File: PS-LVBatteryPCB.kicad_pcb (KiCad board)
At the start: 2 copper layers, 7 parts, among them J1 NTC_01, J2 NTC_02, J3 NTC_OUT, J4 SUPP+, J5 SUPP_GND, J6 SUPP_FUSE

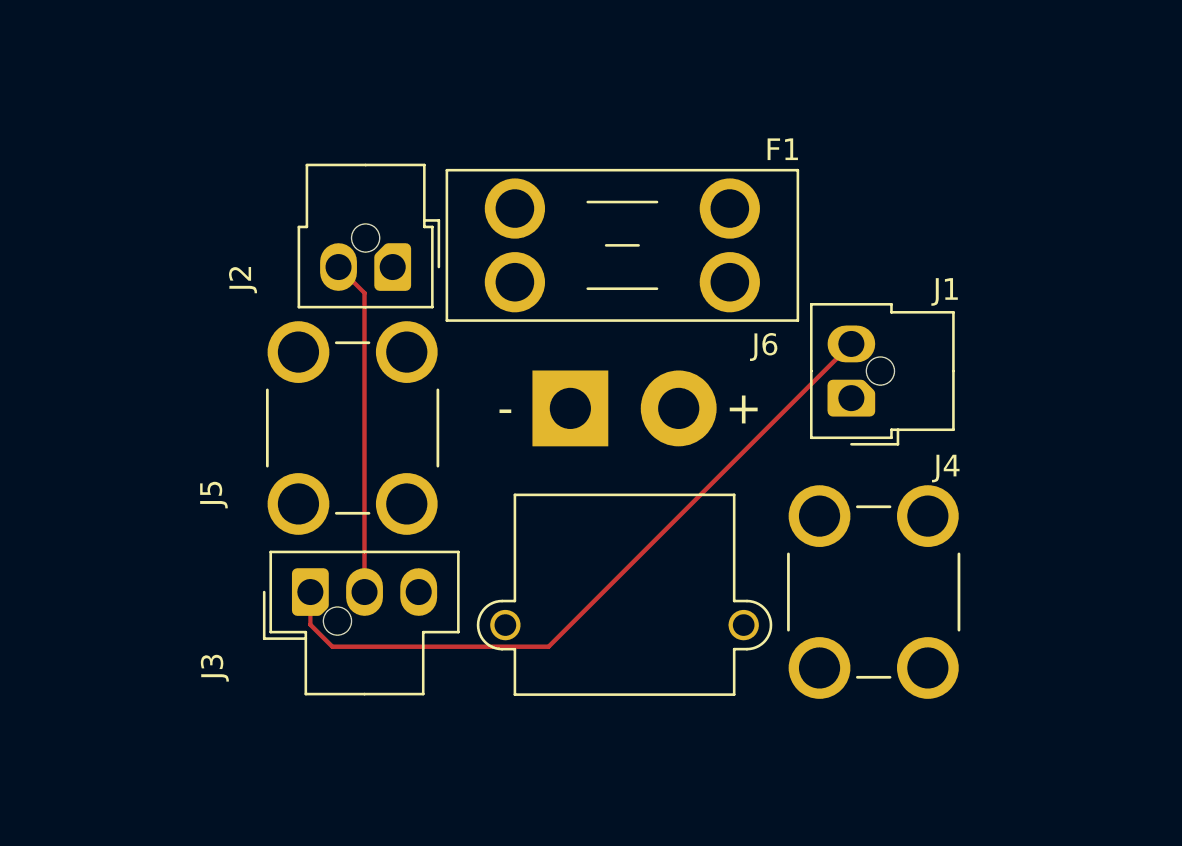
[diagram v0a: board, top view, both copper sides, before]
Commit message: Added all fp's, added edge and planes, added traces, lots of errors
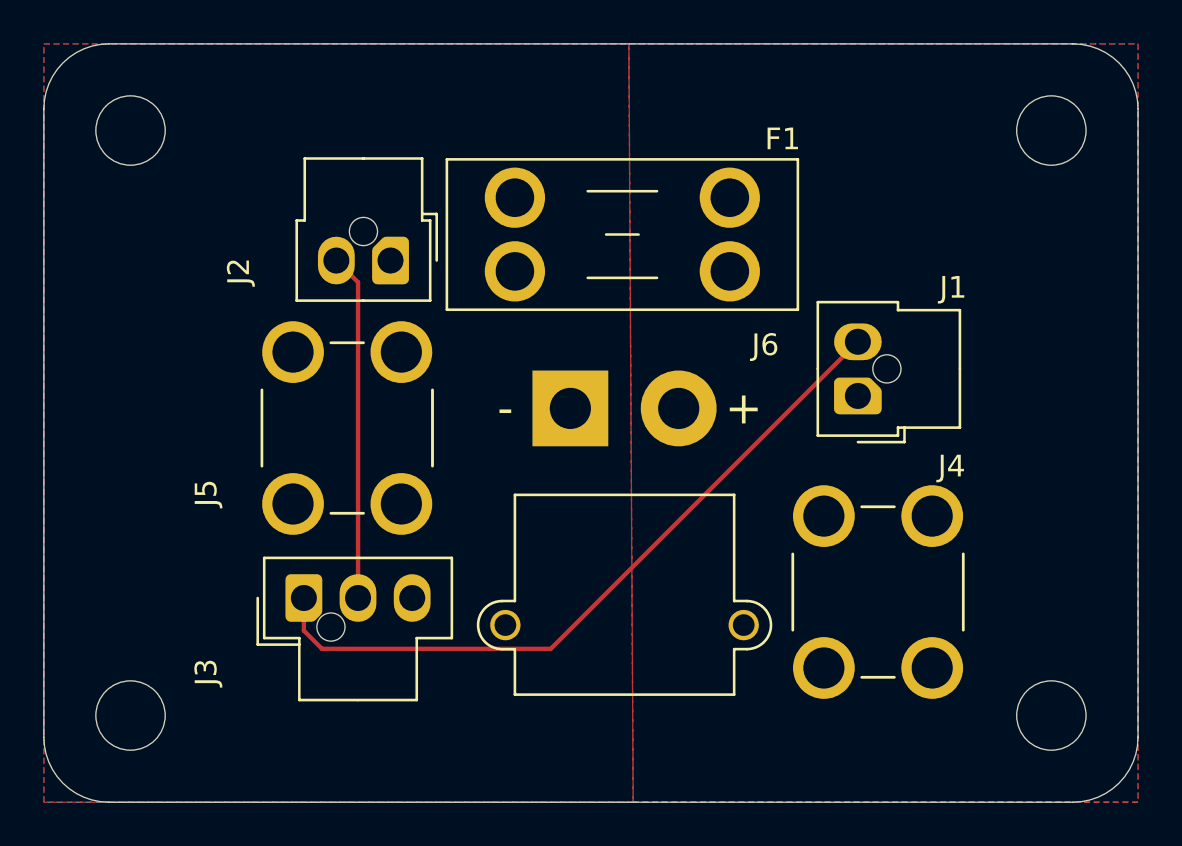
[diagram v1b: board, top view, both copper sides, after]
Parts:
- added REF**: MountingHole_3.2mm_M3, MountingHole:MountingHole_3.2mm_M3, F.Cu at (164.0, 109.5)
- added REF**: MountingHole_3.2mm_M3, MountingHole:MountingHole_3.2mm_M3, F.Cu at (121.5, 82.5)
- added REF**: MountingHole_3.2mm_M3, MountingHole:MountingHole_3.2mm_M3, F.Cu at (121.5, 109.5)
- added REF**: MountingHole_3.2mm_M3, MountingHole:MountingHole_3.2mm_M3, F.Cu at (164.0, 82.5)
- moved F1 0.50 mm to (139.2, 85.6)
- moved J3 0.41 mm to (129.5, 104.1)
- moved J2 0.32 mm to (133.5, 88.5)
- moved J1 0.32 mm to (155.1, 94.8)
- moved J5 0.25 mm to (131.5, 96.2)
- moved J4 0.20 mm to (156.0, 103.8)
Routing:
- net Net-(J1-Pin_2): track 32.7 -> 33.3 mm
- added copper zone on F.Cu, net /SUPP+
- added copper zone on F.Cu, net /SUPP_FUSE+
- added copper zone on B.Cu, net /SUPP_GND
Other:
- board outline added: 50.5 x 35 mm

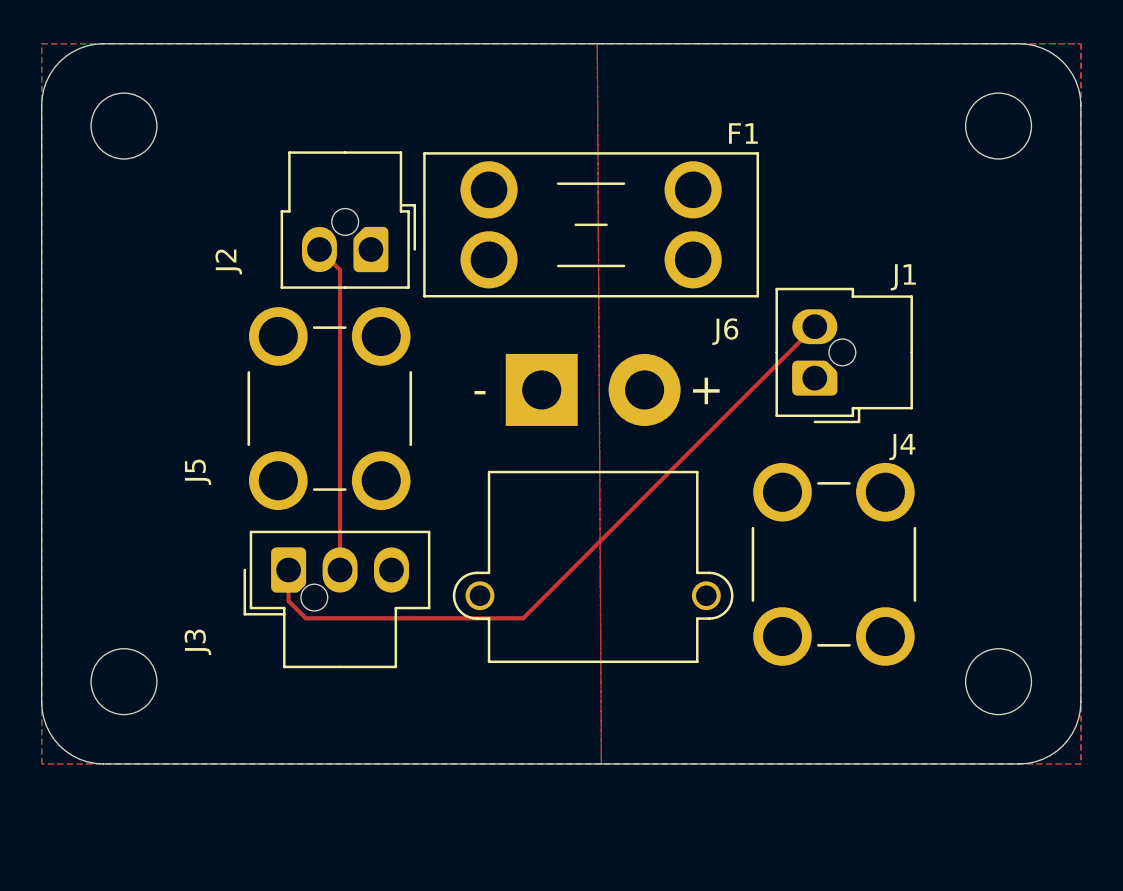
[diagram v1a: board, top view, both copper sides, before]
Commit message: reorganized pcb and changed up fp's
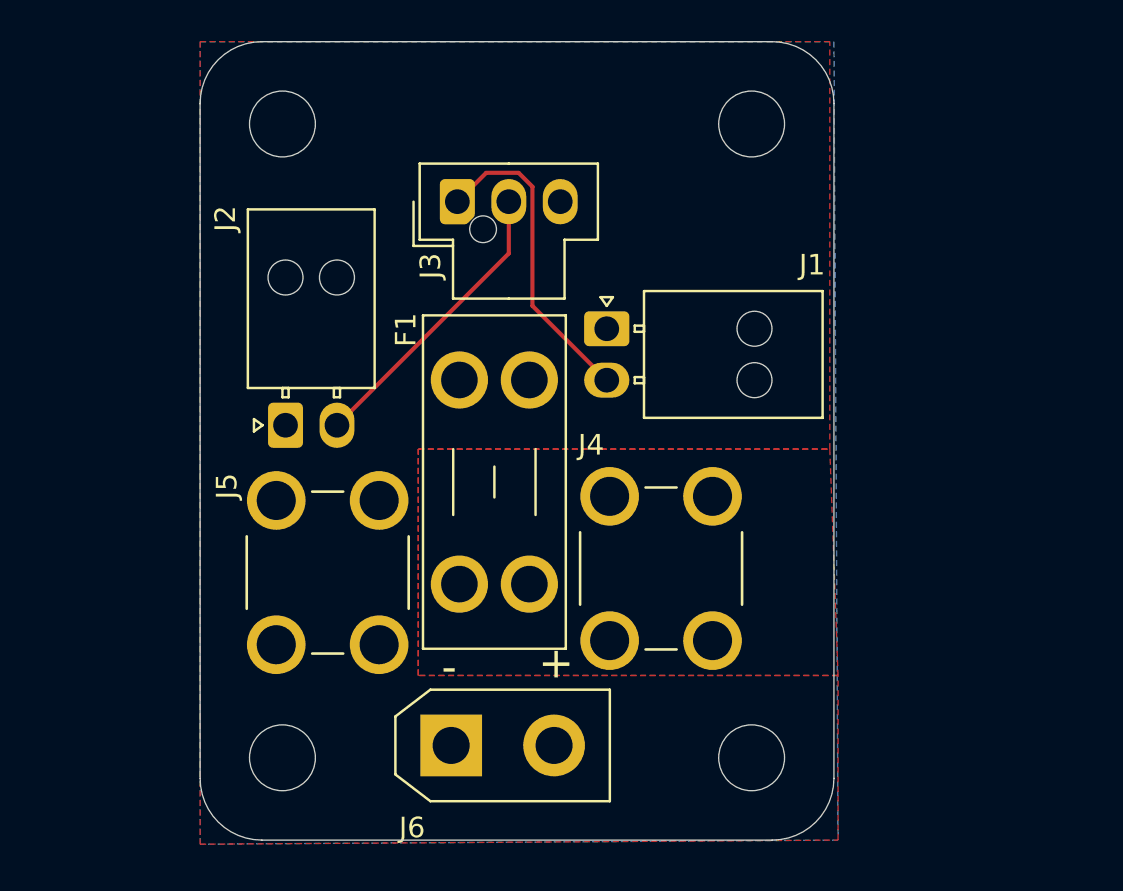
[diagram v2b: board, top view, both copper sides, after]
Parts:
- J1, J2: footprint UTSVT_Connectors:Molex_Nano-Fit_105309-xx02_1x02_P2.50mm_Vertical -> Connector_Molex:Molex_Nano-Fit_105313-xx02_1x02_P2.50mm_Horizontal
- J6: footprint UTSVT_Connectors:AMASS_XT30PW-M_1x02_P2.50mm_Horizontal -> UTSVT_Connectors:AMASS_XT30UPB-M_1x02_P5.0mm_Vertical
- moved J3 19.7 mm to (137.7, 86.2)
- moved J6 17.8 mm to (137.4, 112.6), turned to 0 degrees
- moved REF** 12.6 mm to (152.0, 113.2)
- moved REF** 12.0 mm to (152.0, 82.4)
- moved J1 10.4 mm to (145.0, 92.3), turned to 0 degrees
- moved J2 9.49 mm to (129.3, 97.0), turned to 90 degrees
- moved F1 9.45 mm to (141.2, 94.8), turned to -90 degrees
- moved REF** 8.54 mm to (129.2, 113.2)
- moved J4 8.40 mm to (147.6, 104.0)
- moved J5 7.97 mm to (131.4, 104.2)
- moved REF** 7.70 mm to (129.2, 82.4)
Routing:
- net Net-(J1-Pin_2): track 33.3 -> 15.4 mm
- net Net-(J2-Pin_2): track 16.0 -> 14.3 mm
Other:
- board size 50.5 x 35 mm -> 30.8 x 38.8 mm

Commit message: reorganize and added SOME 3D models
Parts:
- moved J1 11.8 mm to (145.0, 104.2)
- moved REF** 10.0 mm to (139.0, 80.2)
- moved J4 9.85 mm to (151.6, 95.0)
- moved REF** 2.20 mm to (152.0, 80.2)
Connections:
- F1 pad 1: /SUPP_FUSE+ -> /SUPP+
- F1 pad 2: /SUPP+ -> /SUPP_FUSE+
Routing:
- net Net-(J1-Pin_2): track 15.4 -> 27.2 mm
- removed copper zone on F.Cu, net /SUPP+
- removed copper zone on F.Cu, net /SUPP_FUSE+
- removed copper zone on B.Cu, net /SUPP_GND
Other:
- board size 30.8 x 38.8 mm -> 30.8 x 41 mm

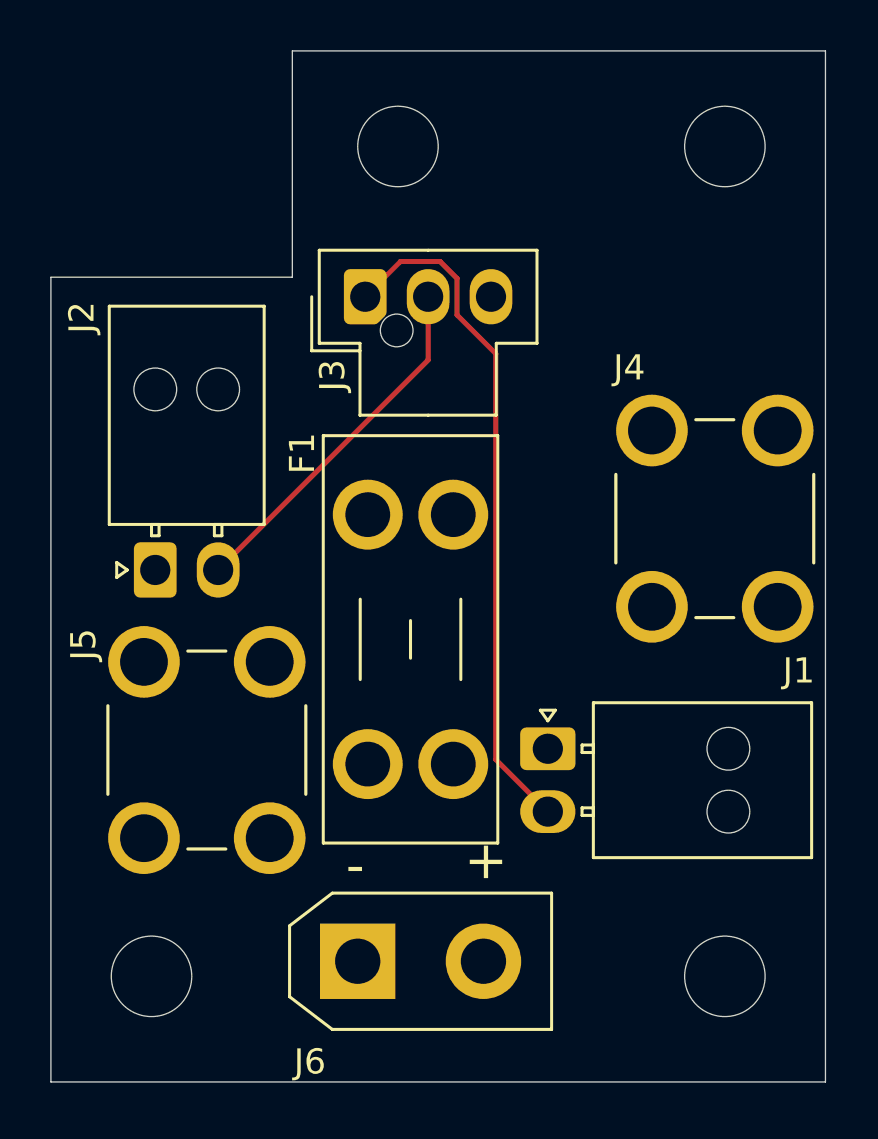
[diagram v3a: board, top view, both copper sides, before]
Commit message: reorganized layout, gotta add planes
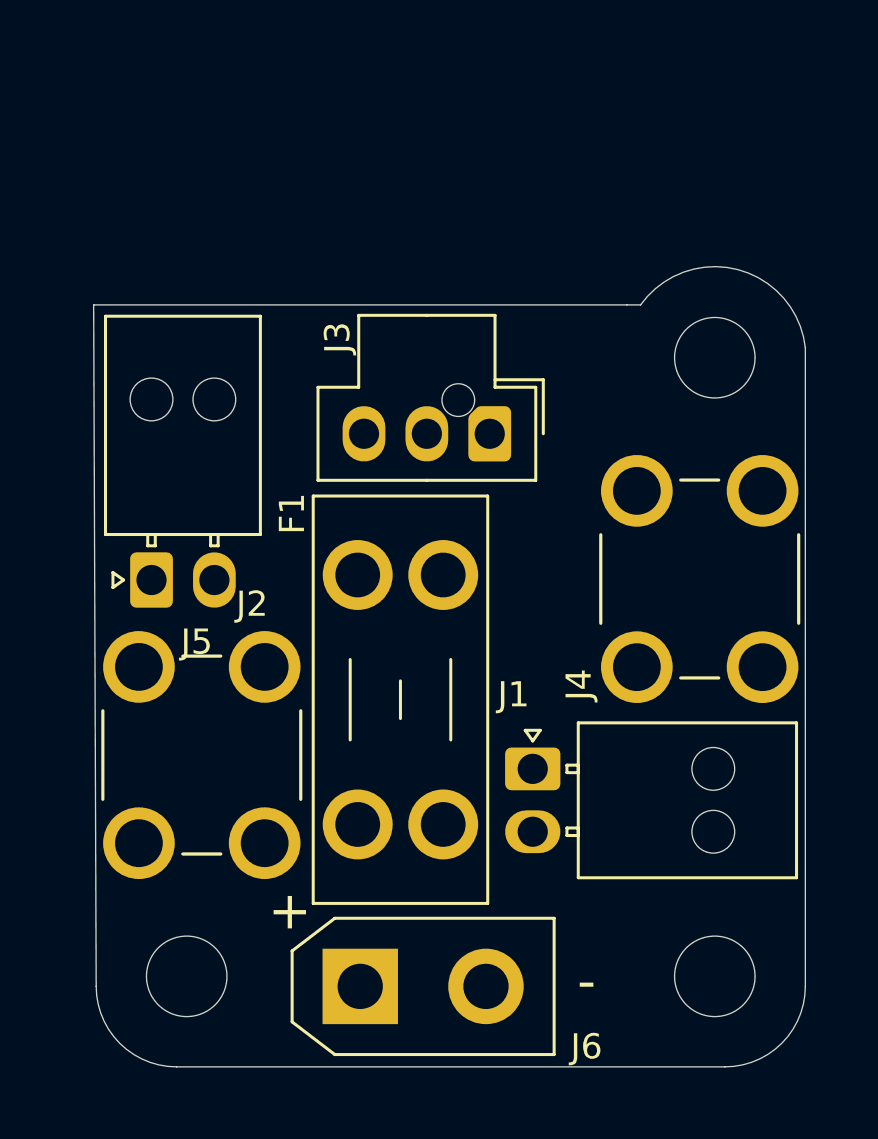
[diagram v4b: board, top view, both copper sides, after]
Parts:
- removed the REF** at (139.0, 80.2)
- moved REF** 8.41 mm to (151.6, 88.6)
- moved J3 7.36 mm to (142.7, 91.6), turned to -90 degrees
- moved J4 2.47 mm to (151.0, 97.4)
- moved F1 2.43 mm to (140.8, 97.2)
- moved REF** 1.40 mm to (130.6, 113.2)
- moved J6 1.00 mm to (137.5, 113.6)
- moved J1 1.00 mm to (144.4, 105.0)
- moved J2 0.43 mm to (129.2, 97.4)
- moved REF** 0.40 mm to (151.6, 113.2)
- moved J5 0.28 mm to (131.2, 104.4)
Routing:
- net Net-(J1-Pin_2): track 27.2 -> 0.00 mm
- net Net-(J2-Pin_2): track 14.3 -> 0.00 mm
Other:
- board size 30.8 x 41 mm -> 28.3 x 31.8 mm

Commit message: R1
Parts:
- moved REF** 0.26 mm to (130.7, 113.0)
- moved REF** 0.22 mm to (151.5, 113.0)
- moved J1 0.19 mm to (144.2, 104.8)
- moved REF** 0.16 mm to (151.6, 88.8)
- moved F1 0.10 mm to (140.7, 97.2)
- moved J5 0.10 mm to (131.2, 104.3)
- moved J3 0.09 mm to (142.6, 91.7)
- moved J4 0.07 mm to (150.9, 97.4)
- moved J2 0.07 mm to (129.2, 97.5)
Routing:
- net Net-(J1-Pin_2): track 0.00 -> 37.2 mm
- net Net-(J1-Pin_1): track 0.00 -> 31.7 mm
- net Net-(J2-Pin_2): track 0.00 -> 11.9 mm
- added copper zone on F.Cu, net /SUPP+
- added copper zone on F.Cu, net /SUPP_FUSE+
- added copper zone on B.Cu, net /SUPP_GND
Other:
- board size 28.3 x 31.8 mm -> 28.2 x 31.4 mm

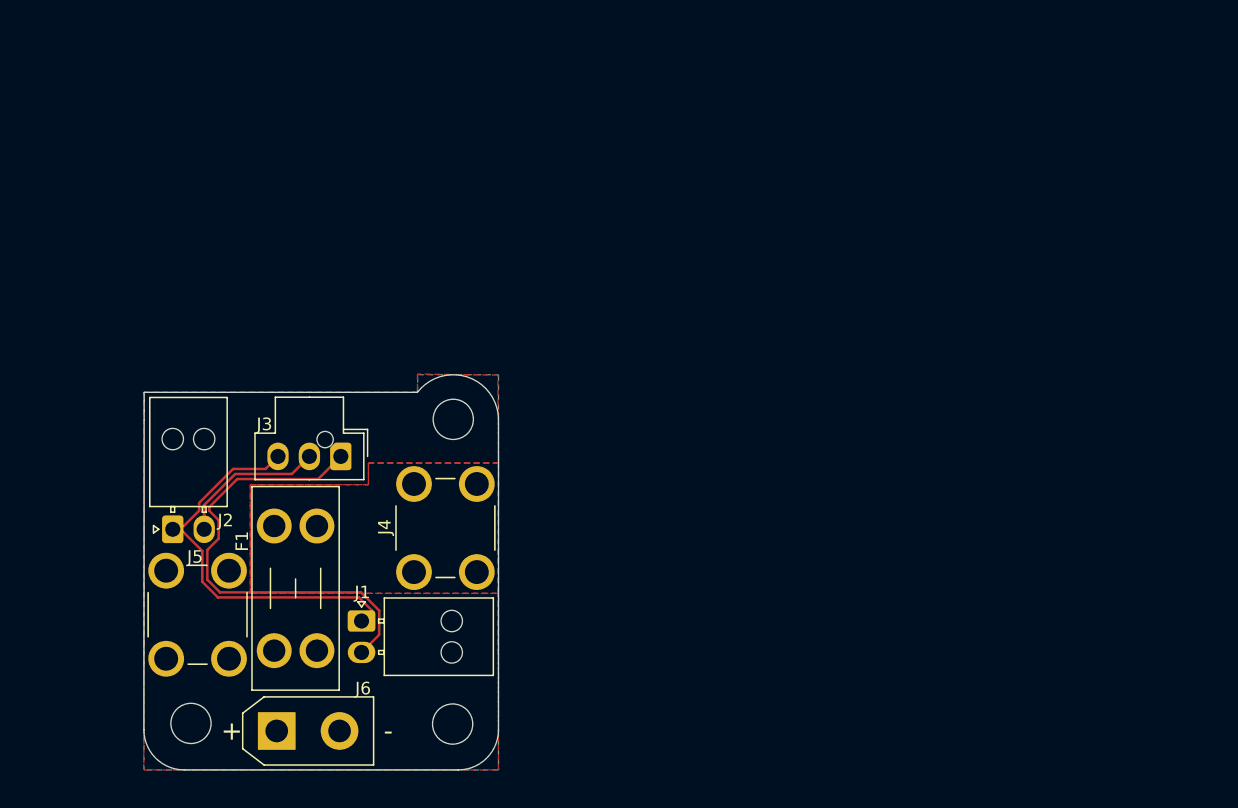
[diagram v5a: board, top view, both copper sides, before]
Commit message: thinner layout
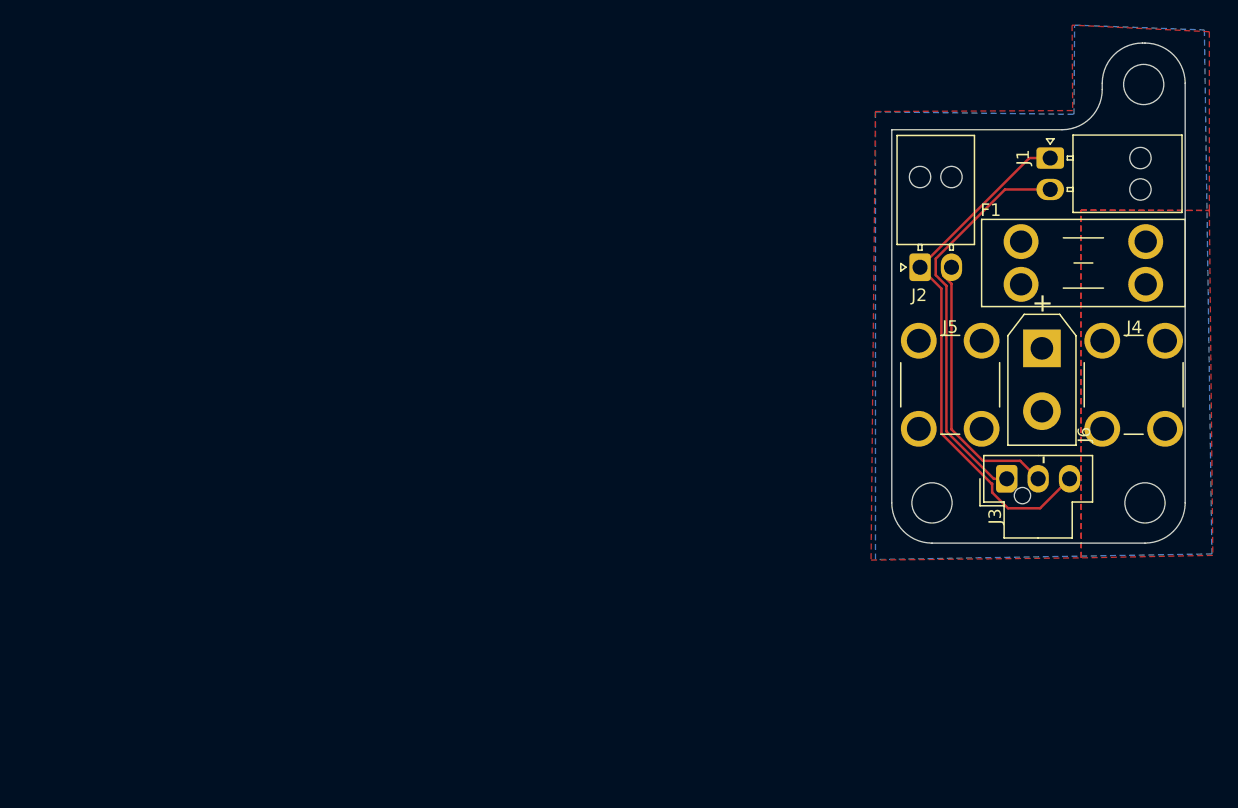
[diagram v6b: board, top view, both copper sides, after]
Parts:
- moved REF** 77.9 mm to (206.6, 95.4)
- moved F1 68.7 mm to (206.7, 78.0), turned to 180 degrees
- moved J6 68.1 mm to (198.4, 83.1), turned to -90 degrees
- moved J1 66.0 mm to (199.1, 68.0)
- moved J2 63.0 mm to (188.7, 76.6)
- moved J5 62.6 mm to (191.1, 86.0)
- moved REF** 61.1 mm to (206.5, 62.1)
- moved J4 55.9 mm to (205.7, 86.0)
- moved J3 53.0 mm to (195.6, 93.5), turned to 90 degrees
- moved REF** 42.0 mm to (189.7, 95.4)
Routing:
- net Net-(J1-Pin_1): track 31.7 -> 41.9 mm
- net Net-(J2-Pin_2): track 11.9 -> 22.0 mm
- net Net-(J1-Pin_2): track 37.2 -> 31.9 mm
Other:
- board size 28.2 x 31.4 mm -> 23.4 x 39.8 mm
